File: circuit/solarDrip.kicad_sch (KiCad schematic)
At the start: 25 parts, among them J1 DCDC_01x03_Socket, J2 MPPT_01x04_Pin, J3 solar_panel, J4 battery, J5 soil_moisture, J6 water_level, J7 pump, J8 USB_C_Receptacle_USB2.0_14P, Q1 2N7002E, Q2 2N7002E, Q3 FDN340P, U1 ESP32-C3-WROOM-02

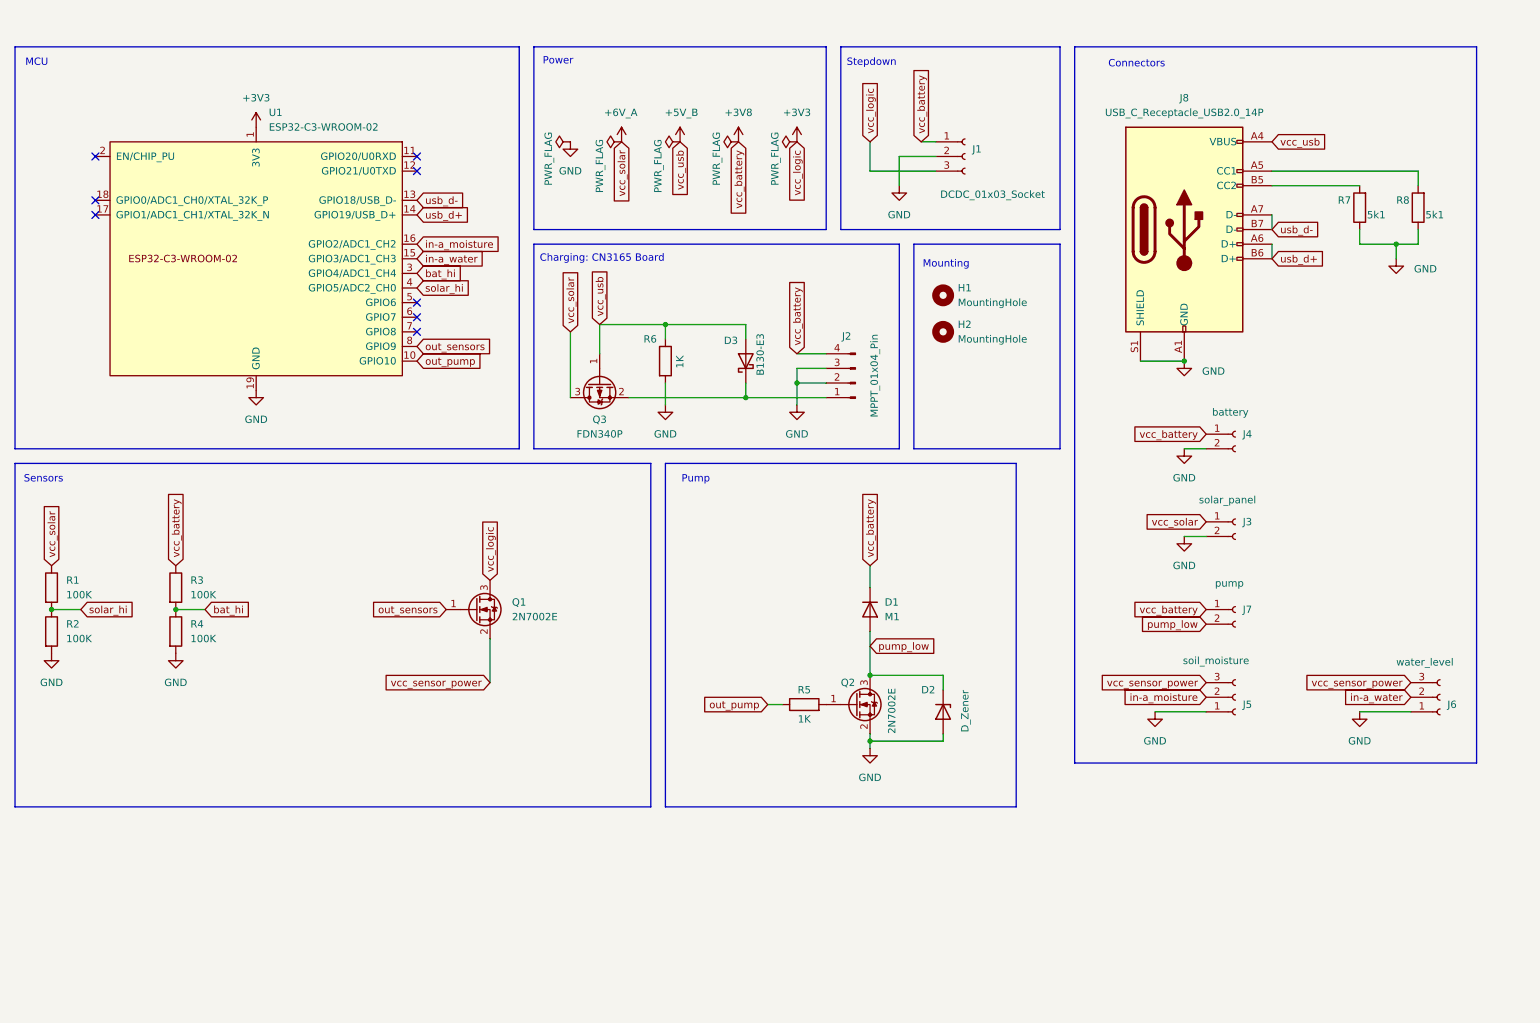
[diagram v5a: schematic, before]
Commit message: add s annotations
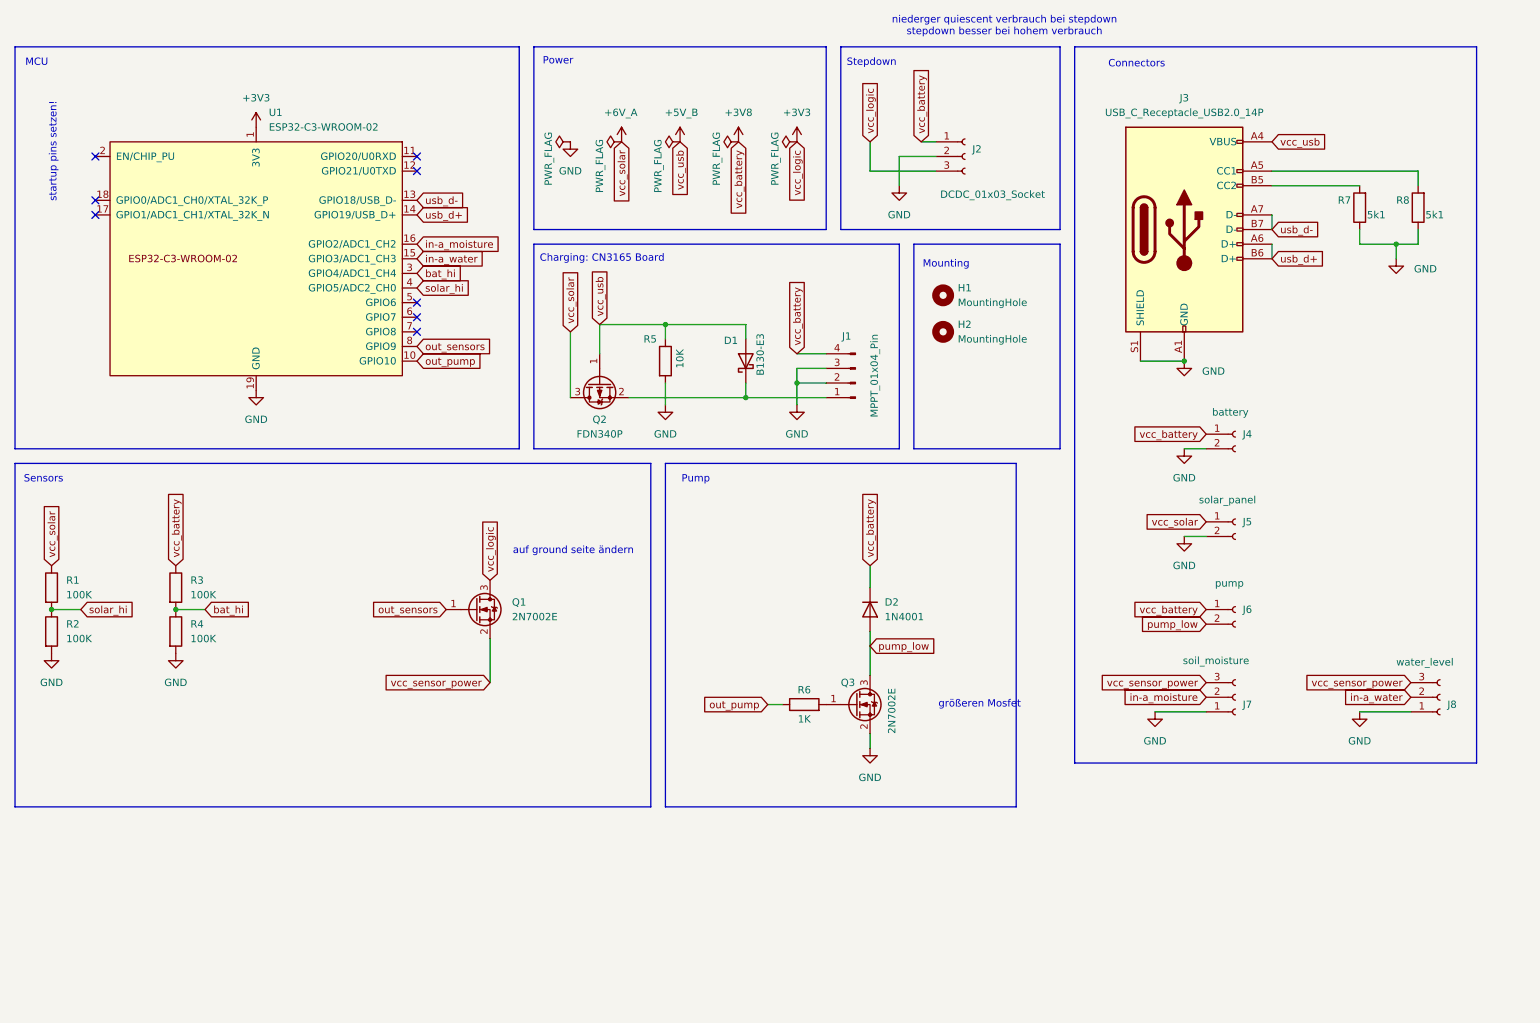
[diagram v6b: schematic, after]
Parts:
- removed D2: D_Zener, symbol Device:D_Zener
- D2: renamed from D1; value M1 -> 1N4001
- R5: renamed from R6; value 1K -> 10K
- R7, R8: footprint (none) -> Resistor_SMD:R_0402_1005Metric_Pad0.72x0.64mm_HandSolder
- renumbered D3 to D1, J2 to J1, J1 to J2, J8 to J3, J3 to J5, J7 to J6, J5 to J7, J6 to J8, Q3 to Q2, Q2 to Q3, R5 to R6
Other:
- note added: "auf ground seite ändern"
- note added: "größeren Mosfet"
- note added: "niederger quiescent verbrauch bei stepdown stepdown besser bei hohem verbrauch"
- note added: "startup pins setzen!"

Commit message: init supermini variant
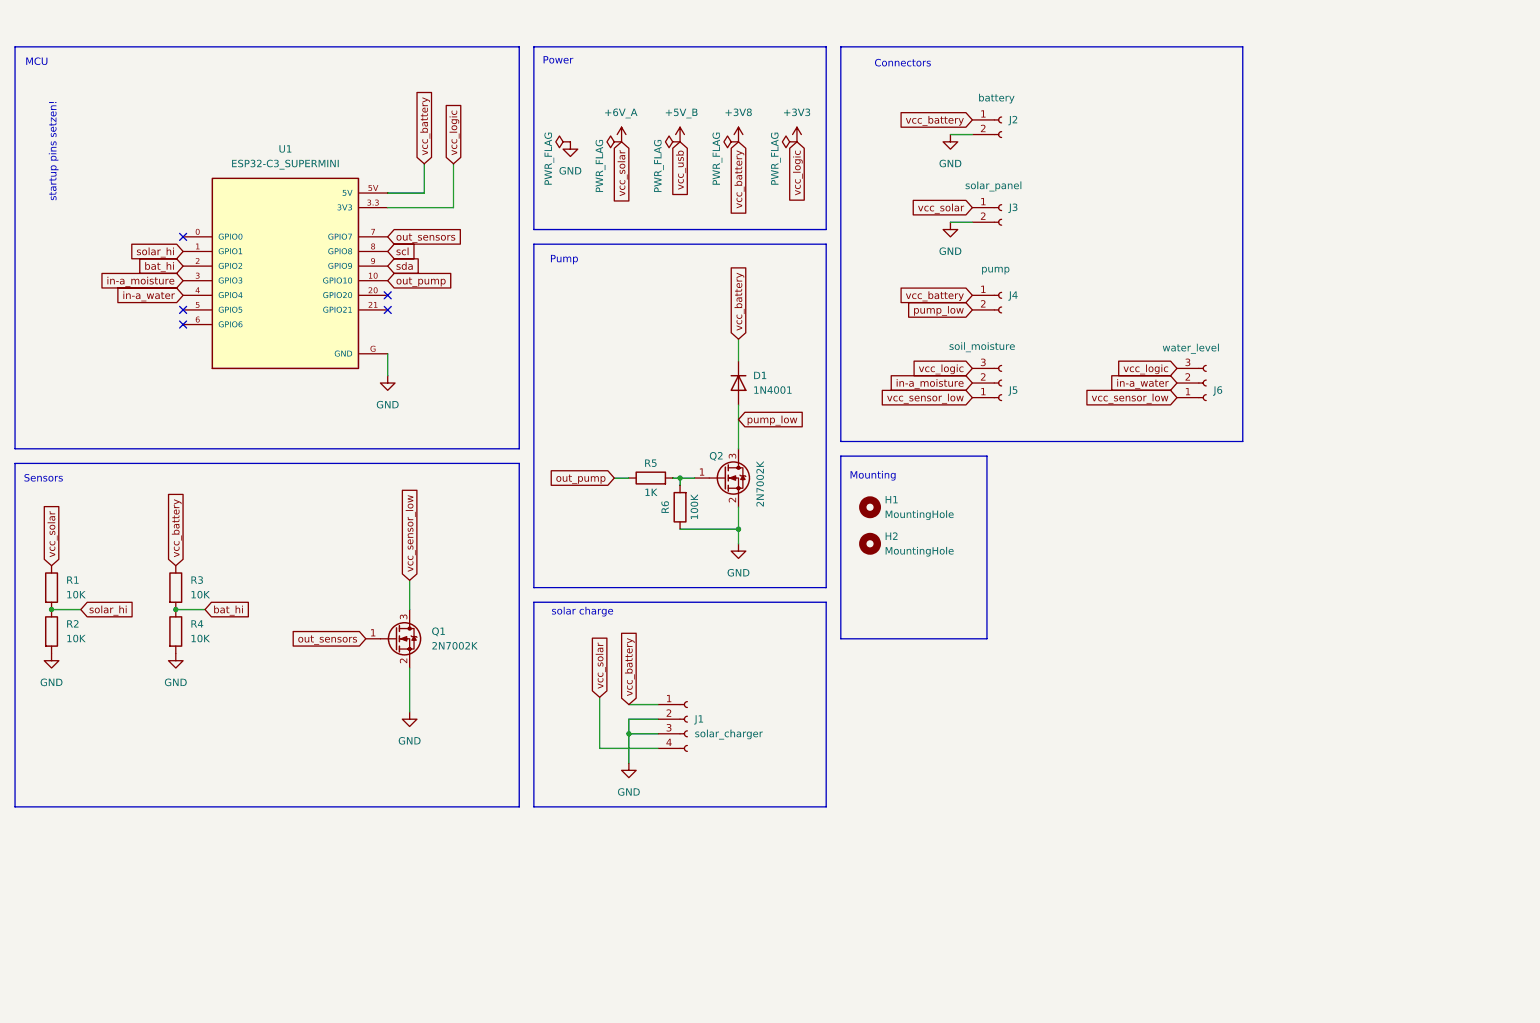
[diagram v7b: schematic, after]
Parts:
- removed D1: B130-E3, Diode_SMD:D_SMA, symbol Diode:B130-E3
- removed J1: MPPT_01x04_Pin, Connector_PinHeader_2.54mm:PinHeader_1x04_P2.54mm_Vertical, symbol Connector:Conn_01x04_Pin
- removed J2: DCDC_01x03_Socket, Connector_PinHeader_2.54mm:PinHeader_1x03_P2.54mm_Vertical, symbol Connector:Conn_01x03_Socket
- removed J3: USB_C_Receptacle_USB2.0_14P, Connector_USB:USB_C_Receptacle_G-Switch_GT-USB-7010ASV, symbol Connector:USB_C_Receptacle_USB2.0_14P
- removed Q2: FDN340P, Package_TO_SOT_SMD:SOT-23, symbol Transistor_FET:FDN340P
- removed R5: 10K, Resistor_SMD:R_0402_1005Metric_Pad0.72x0.64mm_HandSolder, symbol Device:R
- removed R7, R8: 5k1, Resistor_SMD:R_0402_1005Metric_Pad0.72x0.64mm_HandSolder, symbol Device:R
- removed U1: ESP32-C3-WROOM-02, espressiv_git:ESP32-C3-WROOM-02, symbol espressiv_git:ESP32-C3-WROOM-02
- added J1: solar_charger, Connector_PinSocket_2.54mm:PinSocket_1x04_P2.54mm_Vertical, symbol Connector:Conn_01x04_Socket
- added R6: 100K, Resistor_SMD:R_0402_1005Metric_Pad0.72x0.64mm_HandSolder, symbol Device:R
- added U1: ESP32-C3_SUPERMINI, supermini:MODULE_ESP32-C3_SUPERMINI, symbol esp32c3_supermini:ESP32-C3_SUPERMINI
- Q1: value 2N7002E -> 2N7002K
- Q2: renamed from Q3; value 2N7002E -> 2N7002K
- R1, R2, R3, R4: value 100K -> 10K
- renumbered D2 to D1, J4 to J2, J5 to J3, J6 to J4, J7 to J5, J8 to J6, R6 to R5
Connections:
- net +3V3: now also J5.3 (Pin_3), J6.3 (Pin_3), U1.3.3 (3V3); no longer Q1.3 (D)
- net +3V8: now also J1.1 (Pin_1), U1.5V
- net +6V_A: now also J1.4 (Pin_4)
- net GND: now also Q1.2 (S), J1.2 (Pin_2), J1.3 (Pin_3), R6.1, U1.G (GND); no longer J5.1 (Pin_1), J6.1 (Pin_1)
- net bat_hi: now also U1.2 (GPIO2)
- net in-a_moisture: now also U1.3 (GPIO3)
- net in-a_water: now also U1.4 (GPIO4)
- net out_pump: now also U1.10 (GPIO10)
- net out_sensors: now also U1.7 (GPIO7)
- net solar_hi: now also U1.1 (GPIO1)
- net at Q2.1 (G), R5.2: now also R6.2
- removed net vcc_sensor_power: J5.3 (Pin_3), J6.3 (Pin_3), Q1.2 (S)
- new net scl: U1.8 (GPIO8)
- new net sda: U1.9 (GPIO9)
- new net vcc_sensor_low: J5.1 (Pin_1), J6.1 (Pin_1), Q1.3 (D)
- no-connect marks 8 -> 5
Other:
- note added: "solar charge"
- note removed: "Charging: CN3165 Board"
- note removed: "Stepdown"
- note removed: "auf ground seite ändern"
- note removed: "größeren Mosfet"
- note removed: "niederger quiescent verbrauch bei stepdown stepdown besser bei hohem verbrauch"
- moved on the sheet: D1, H1, H2, J2, J3, J4, J5, J6, Q1, Q2, R5

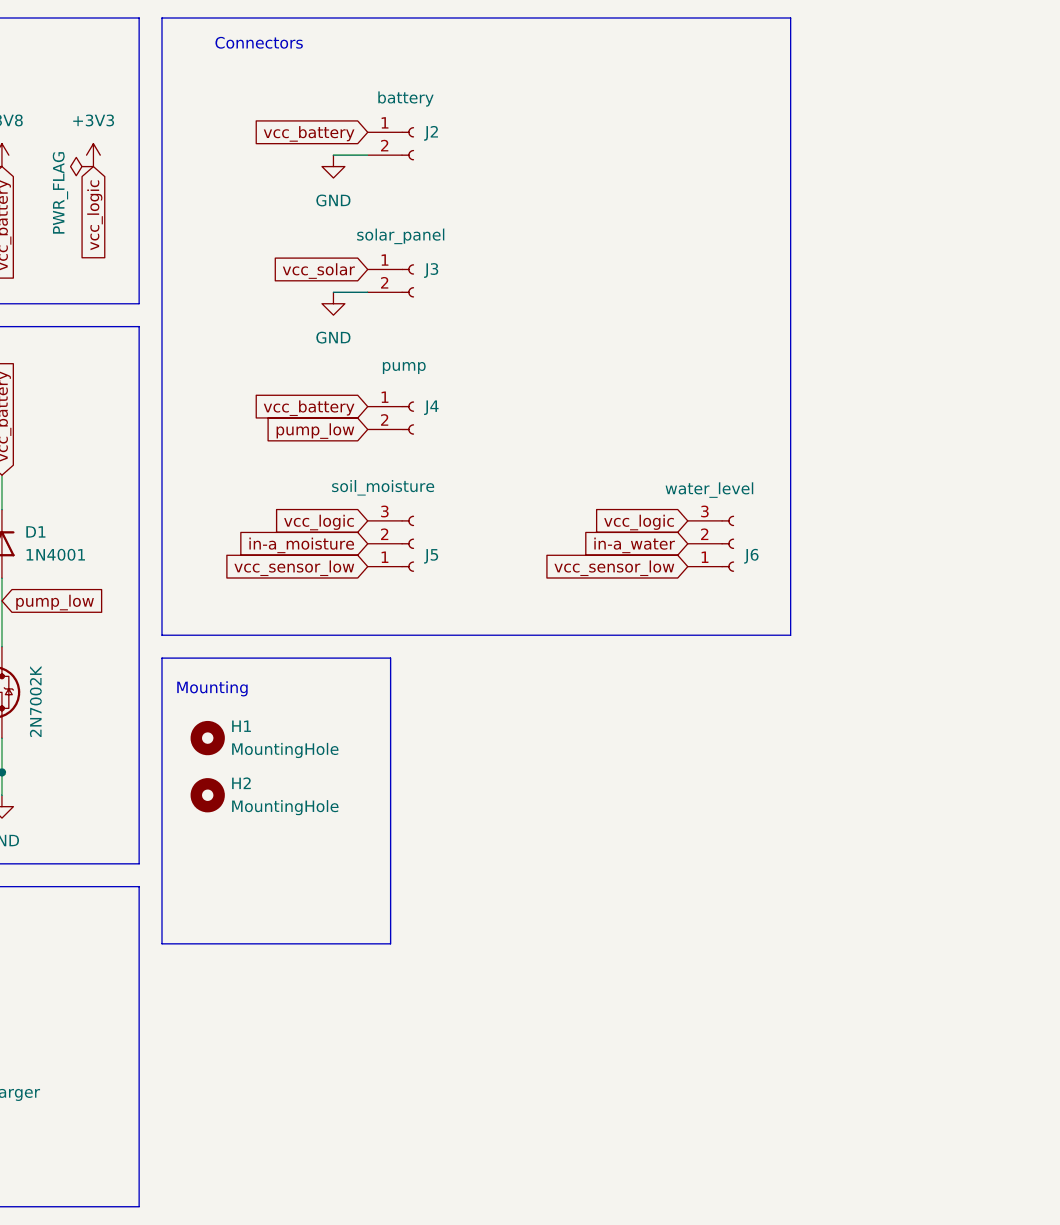
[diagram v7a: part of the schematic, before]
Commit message: add usb_charging
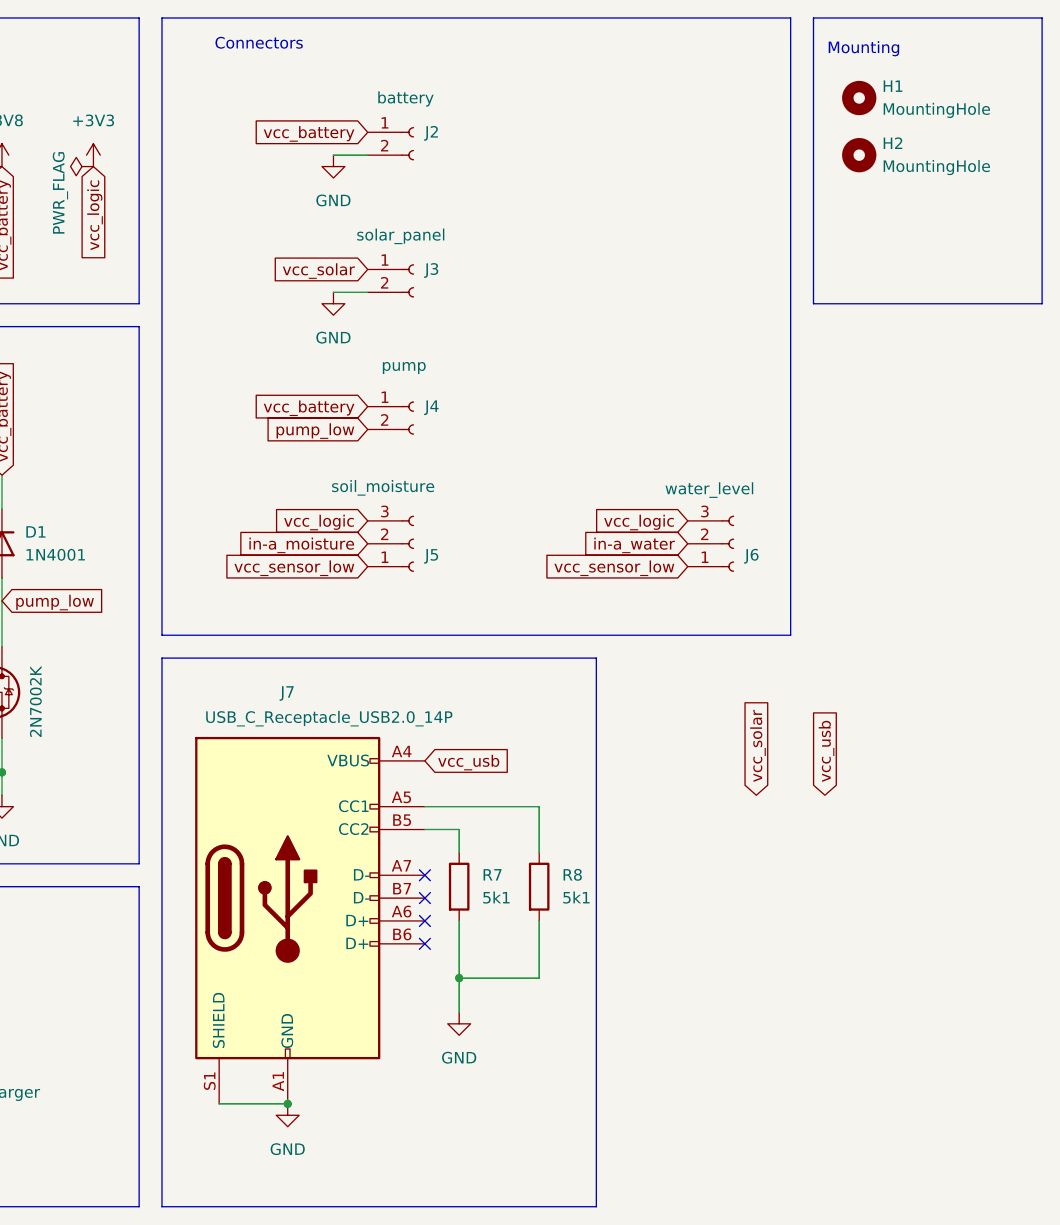
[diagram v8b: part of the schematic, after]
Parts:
- added J7: USB_C_Receptacle_USB2.0_14P, symbol Connector:USB_C_Receptacle_USB2.0_14P
- added R7, R8: 5k1, symbol Device:R
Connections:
- net +5V_B: now also J7.A4 (VBUS), J7.A9 (VBUS), J7.B4 (VBUS), J7.B9 (VBUS)
- net GND: now also J7.A1 (GND), J7.A12 (GND), J7.B1 (GND), J7.B12 (GND), J7.S1 (SHIELD), R7.2, R8.2
- new net: J7.A5 (CC1), R8.1
- new net: J7.B5 (CC2), R7.1
- no-connect marks 5 -> 9
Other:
- moved on the sheet: H1, H2
